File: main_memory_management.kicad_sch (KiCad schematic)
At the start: 21 parts

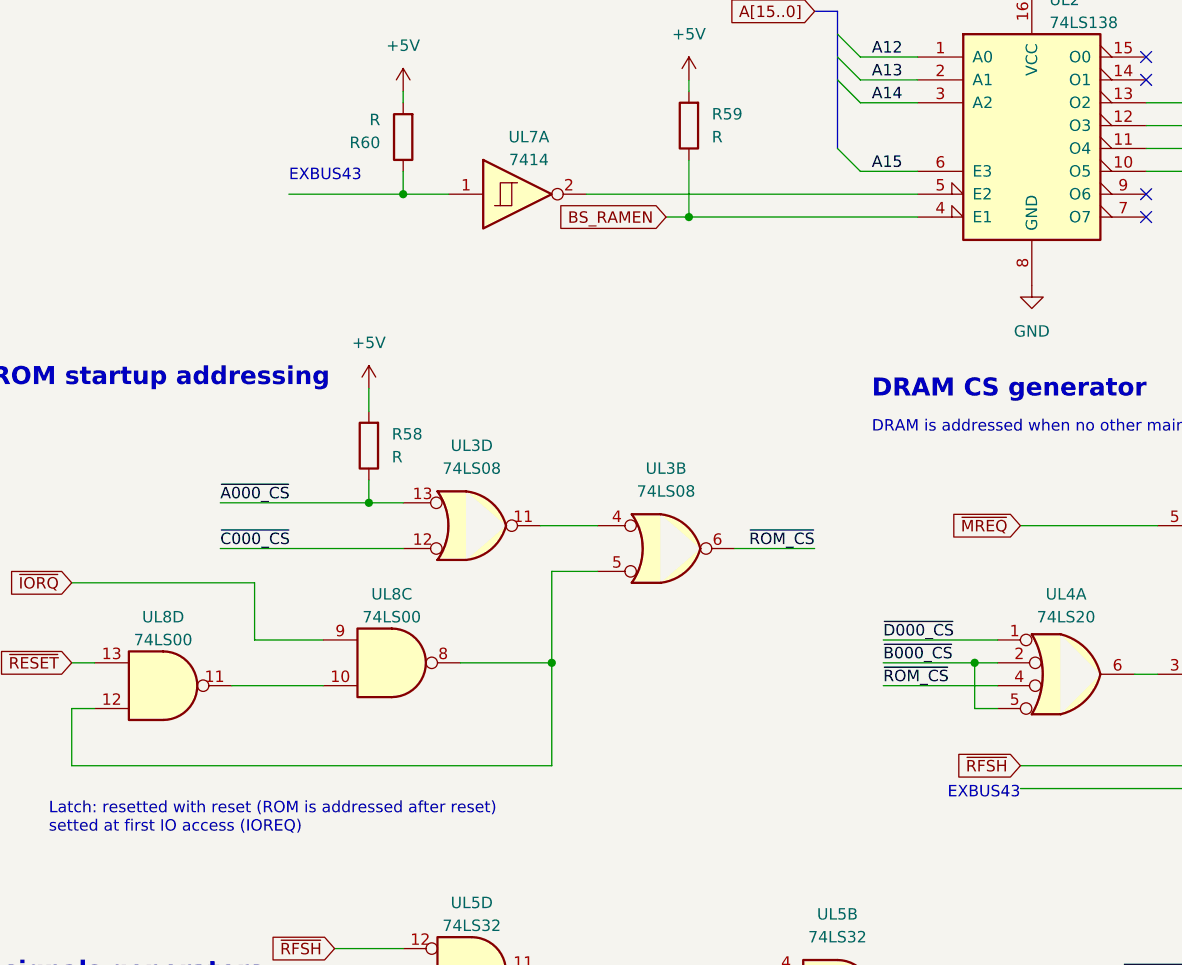
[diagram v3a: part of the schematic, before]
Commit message: pcb: added all the connector, 99% routed
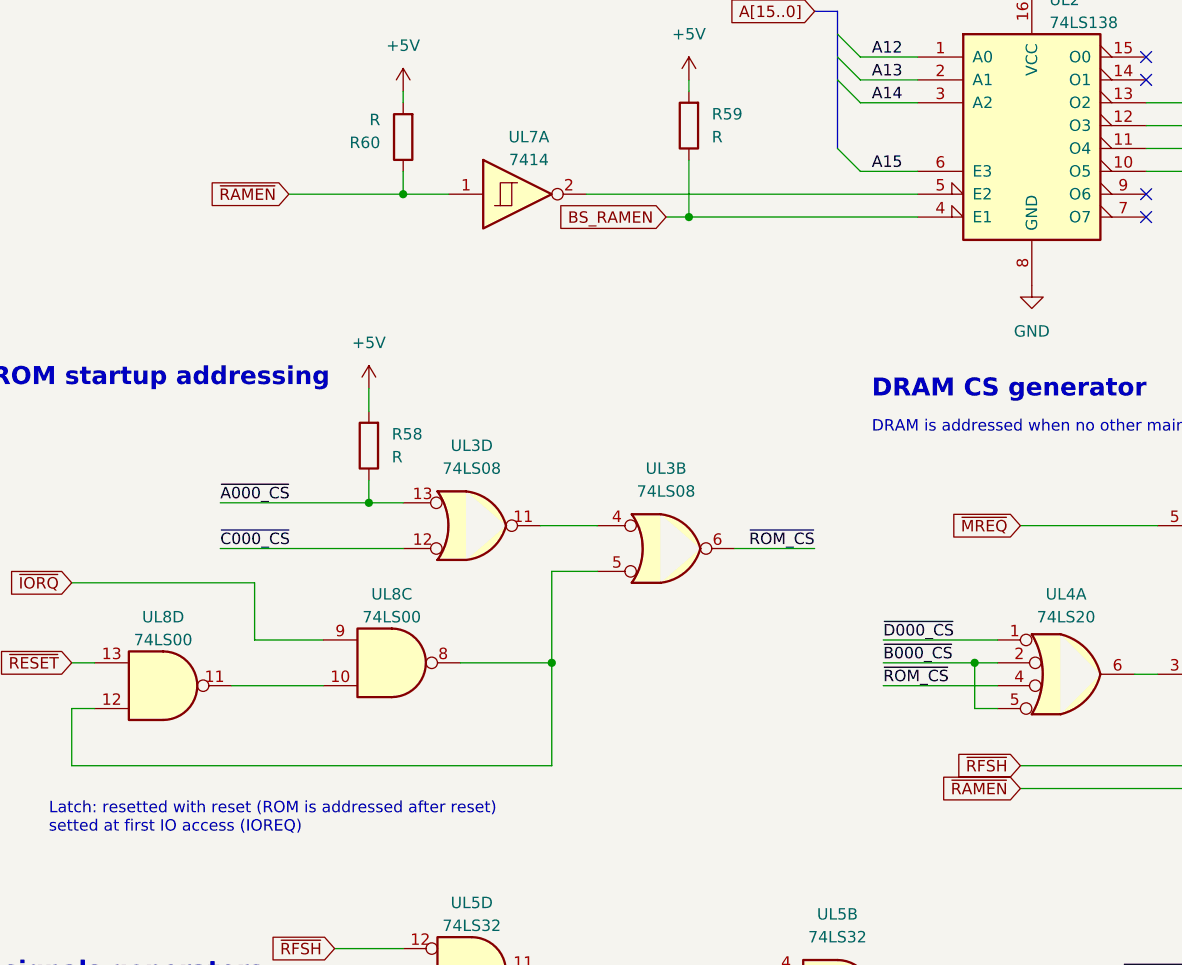
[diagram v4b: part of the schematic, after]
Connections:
- net ~{RAMEN}: now reaches UL4.13
- net ~{RAMEN}: now also R60.1, UL7.1
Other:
- note removed: "EXBUS43"
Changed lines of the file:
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@@
 		)
 	)
-	(text "EXBUS43\n"
-		(exclude_from_sim no)
-		(at 132.08 46.99 0)
-		(effects
-			(font
-				(size 1.27 1.27)
-			)
-			(justify left bottom)
-		)
-	)
 	(text "DRAM CS generator"
 		(exclude_from_sim no)
@@
 		)
 	)
-	(text "EXBUS43"
-		(exclude_from_sim no)
-		(at 213.36 115.57 0)
-		(effects
-			(font
-				(size 1.27 1.27)
-			)
-			(justify right bottom)
-		)
-	)
 	(text "DRAM is addressed when no other main memory are addressed"
 		(exclude_from_sim no)
@@
 		)
 	)
+	(global_label "~{RAMEN}"
+		(shape input)
+		(at 132.08 48.26 180)
+		(fields_autoplaced yes)
+		(effects
+			(font
+				(size 1.27 1.27)
+			)
+			(justify right)
+		)
+		(property "Intersheetrefs" "${INTERSHEET_REFS}"
+			(at 122.8053 48.26 0)
+			(effects
+				(font
+					(size 1.27 1.27)
+				)
+				(justify right)
+				(hide yes)
+			)
+		)
+	)
 	(global_label "~{RAS}"
 		(shape output)
@@
 			(effects
 				(font
+					(size 1.27 1.27)
+				)
+				(justify right)
+				(hide yes)
+			)
+		)
+	)
+	(global_label "~{RAMEN}"
+		(shape input)
+		(at 213.36 114.3 180)
+		(fields_autoplaced yes)
+		(effects
+			(font
+				(size 1.27 1.27)
+			)
+			(justify right)
+		)
+		(property "Intersheetrefs" "${INTERSHEET_REFS}"
+			(at 204.0853 114.3 0)
+			(effects
+				(font

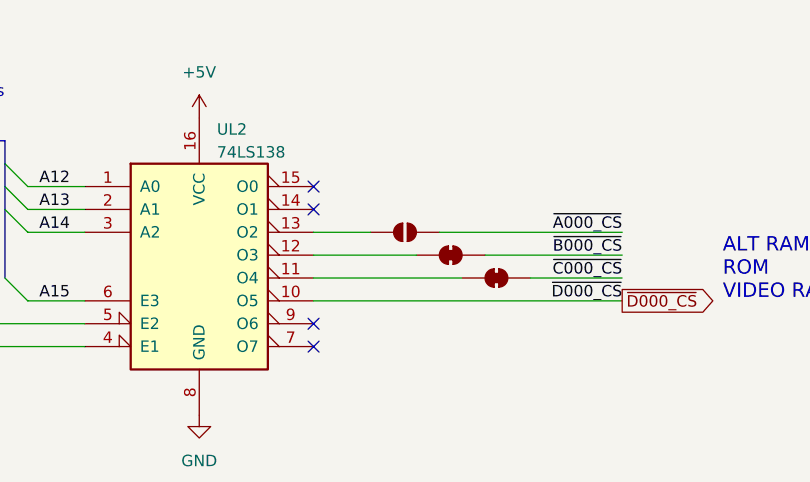
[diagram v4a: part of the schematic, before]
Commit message: pcb: proper symbols for MAP and MAINCLK
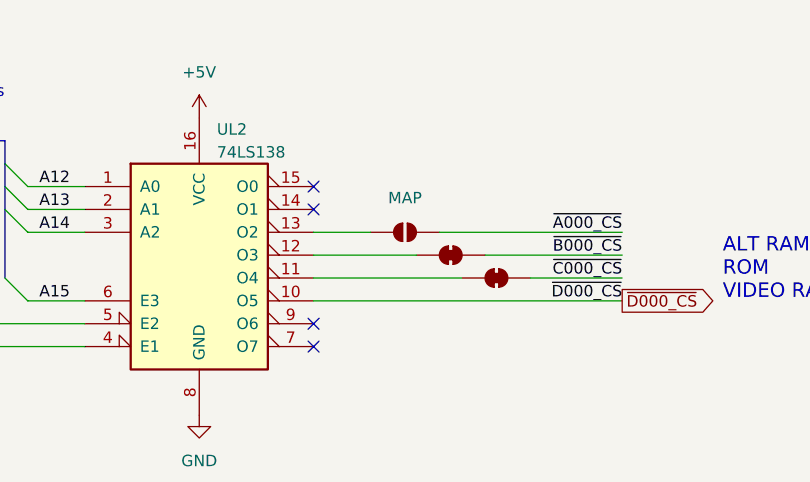
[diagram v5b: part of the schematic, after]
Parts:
- removed MAP1: SolderJumper_2_Open, Connector_PinHeader_2.54mm:PinHeader_2x01_P2.54mm_Vertical, symbol Jumper:SolderJumper_2_Open
- removed MAP2, MAP3: SolderJumper_2_Bridged, Connector_PinHeader_2.54mm:PinHeader_2x01_P2.54mm_Vertical, symbol Jumper:SolderJumper_2_Bridged
- added JP4: MAP, Ceda:MAP, symbol ceda:MAP
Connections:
- net ~{A000_CS}: now also JP4.2 (B)
- net ~{B000_CS}: now also JP4.4 (D)
- net ~{C000_CS}: now also JP4.6 (F)
- net at UL2.11 (O4): now also JP4.5 (E)
- net at UL2.12 (O3): now also JP4.3 (C)
- net at UL2.13 (O2): now also JP4.1 (A)
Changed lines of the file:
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@@
-	)
-	(symbol
-		(lib_id "Jumper:SolderJumper_2_Open")
-		(at 237.49 38.1 0)
-		(unit 1)
-		(exclude_from_sim no)
-		(in_bom yes)
-		(on_board yes)
-		(dnp no)
-		(fields_autoplaced yes)
-		(property "Reference" "MAP1"
-			(at 238.125 40.64 90)
-			(effects
-				(font
-					(size 1.27 1.27)
-				)
-				(justify right)
-				(hide yes)
-			)
-		)
-		(property "Value" "SolderJumper_2_Open"
-			(at 235.585 40.64 90)
-			(effects
-				(font
-					(size 1.27 1.27)
-				)
-				(justify right)
-				(hide yes)
-			)
-		)
-		(property "Footprint" "Connector_PinHeader_2.54mm:PinHeader_2x01_P2.54mm_Vertical"
-			(at 237.49 38.1 0)
-			(effects
-				(font
-					(size 1.27 1.27)
-				)
-				(hide yes)
-			)
-		)
-		(property "Datasheet" "~"
-			(at 237.49 38.1 0)
-			(effects
-				(font
-					(size 1.27 1.27)
-				)
-				(hide yes)
-			)
-		)
-		(property "Description" ""
-			(at 237.49 38.1 0)
-			(effects
-				(font
-					(size 1.27 1.27)
-				)
-			)
-		)
-		(pin "1"
-		)
-		(pin "2"
-		)
-		(instances
-			(project "ceda"
-				(path "/12a6dbe3-008d-4c5b-88f6-9f1c816060be/4fdb1b90-7ad1-4fa0-9b13-7b81abbda2ba"
-					(reference "MAP1")
-					(unit 1)
-				)
-			)
-		)
 	)
 	(symbol
@@
 	)
 	(symbol
+		(lib_id "ceda:MAP")
+		(at 247.65 43.18 0)
+		(unit 3)
+		(exclude_from_sim no)
+		(in_bom yes)
+		(on_board yes)
+		(dnp no)
+		(fields_autoplaced yes)
+		(property "Reference" "JP4"
+			(at 247.65 36.83 0)
+			(effects
+				(font
+					(size 1.27 1.27)
+				)
+				(hide yes)
+			)
+		)
+		(property "Value" "MAP"
+			(at 247.65 39.37 0)
+			(effects
+				(font
+					(size 1.27 1.27)
+				)
+				(hide yes)
+			)
+		)
+		(property "Footprint" "Ceda:MAP"
+			(at 247.65 39.624 0)
+			(effects
+				(font
+					(size 1.27 1.27)
+				)
+				(hide yes)
+			)
+		)
+		(property "Datasheet" "~"
+			(at 247.65 38.1 0)
+			(effects
+				(font
+					(size 1.27 1.27)
+				)
+				(hide yes)
+			)
+		)
+		(property "Description" ""
+			(at 247.65 43.18 0)
+			(effects
+				(font
+					(size 1.27 1.27)
+				)
+				(hide yes)
+			)
+		)
+		(pin "1"
+		)
+		(pin "6"
+		)
+		(pin "5"
+		)
+		(pin "4"
+		)
+		(pin "3"
+		)
+		(pin "2"
+		)
+		(instances
+			(project ""
+				(path "/12a6dbe3-008d-4c5b-88f6-9f1c816060be/4fdb1b90-7ad1-4fa0-9b13-7b81abbda2ba"
+					(reference "JP4")
+					(unit 3)
+				)
+			)
+		)
+	)
+	(symbol
 		(lib_id "power:+5V")
 		(at 29.21 68.58 90)
@@
 	)
 	(symbol
+		(lib_id "ceda:MAP")
+		(at 242.57 40.64 0)
+		(unit 2)
+		(exclude_from_sim no)
+		(in_bom yes)
+		(on_board yes)
+		(dnp no)
+		(fields_autoplaced yes)
+		(property "Reference" "JP4"
+			(at 242.57 34.29 0)
+			(effects
+				(font
+					(size 1.27 1.27)
+				)
+				(hide yes)
+			)
+		)
+		(property "Value" "MAP"
+			(at 242.57 36.83 0)
+			(effects
+				(font
+					(size 1.27 1.27)
+				)
+				(hide yes)
+			)
+		)
+		(property "Footprint" "Ceda:MAP"
+			(at 242.57 37.084 0)
+			(effects
+				(font
+					(size 1.27 1.27)
+				)
+				(hide yes)
+			)
+		)
+		(property "Datasheet" "~"
+			(at 242.57 35.56 0)
+			(effects
+				(font
+					(size 1.27 1.27)
+				)
+				(hide yes)
+			)
+		)
+		(property "Description" ""
+			(at 242.57 40.64 0)
+			(effects
+				(font
+					(size 1.27 1.27)
+				)
+				(hide yes)
+			)
+		)
+		(pin "1"
+		)
+		(pin "6"
+		)
+		(pin "5"
+		)
+		(pin "4"
+		)
+		(pin "3"
+		)
+		(pin "2"
+		)
+		(instances
+			(project ""
+				(path "/12a6dbe3-008d-4c5b-88f6-9f1c816060be/4fdb1b90-7ad1-4fa0-9b13-7b81abbda2ba"
+					(reference "JP4")
+					(unit 2)
+				)
+			)
+		)
+	)
+	(symbol
 		(lib_id "74xx:74LS14")
 		(at 157.48 48.26 0)
@@
 	)
 	(symbol
-		(lib_id "Jumper:SolderJumper_2_Bridged")
-		(at 247.65 43.18 0)
-		(unit 1)
-		(exclude_from_sim no)
-		(in_bom yes)
-		(on_board yes)
-		(dnp no)
-		(fields_autoplaced yes)
-		(property "Reference" "MAP3"
-			(at 247.65 38.1 0)
-			(effects
-				(font
-					(size 1.27 1.27)
-				)
-				(hide yes)
-			)
-		)
-		(property "Value" "SolderJumper_2_Bridged"
-			(at 247.65 40.64 0)
-			(effects
-				(font
-					(size 1.27 1.27)
-				)
-				(hide yes)
-			)
-		)
-		(property "Footprint" "Connector_PinHeader_2.54mm:PinHeader_2x01_P2.54mm_Vertical"
-			(at 247.65 43.18 0)
-			(effects
-				(font
-					(size 1.27 1.27)
-				)
-				(hide yes)
-			)
-		)
-		(property "Datasheet" "~"
-			(at 247.65 43.18 0)
-			(effects
-				(font
-					(size 1.27 1.27)
-				)
-				(hide yes)
-			)
-		)
-		(property "Description" ""
-			(at 247.65 43.18 0)
-			(effects
-				(font
-					(size 1.27 1.27)
-				)
-			)
-		)
-		(pin "1"
-		)
-		(pin "2"
-		)
-		(instances
-			(project "ceda"
-				(path "/12a6dbe3-008d-4c5b-88f6-9f1c816060be/4fdb1b90-7ad1-4fa0-9b13-7b81abbda2ba"
-					(reference "MAP3")
-					(unit 1)
-				)
-			)
-		)
-	)
-	(symbol
 		(lib_id "power:+5V")
 		(at 144.78 36.83 0)
@@
 	)
 	(symbol
-		(lib_id "Jumper:SolderJumper_2_Bridged")
-		(at 242.57 40.64 0)
-		(unit 1)
-		(exclude_from_sim no)
-		(in_bom yes)
-		(on_board yes)
-		(dnp no)
-		(fields_autoplaced yes)
-		(property "Reference" "MAP2"
-			(at 242.57 35.56 0)
-			(effects
-				(font
-					(size 1.27 1.27)
-				)
-				(hide yes)
-			)
-		)
-		(property "Value" "SolderJumper_2_Bridged"
-			(at 242.57 38.1 0)
-			(effects
-				(font
-					(size 1.27 1.27)
-				)
-				(hide yes)
-			)
-		)
-		(property "Footprint" "Connector_PinHeader_2.54mm:PinHeader_2x01_P2.54mm_Vertical"
-			(at 242.57 40.64 0)
-			(effects
-				(font
-					(size 1.27 1.27)
-				)
-				(hide yes)
-			)
-		)
-		(property "Datasheet" "~"
-			(at 242.57 40.64 0)
-			(effects
-				(font
-					(size 1.27 1.27)
-				)
-				(hide yes)
-			)
-		)
-		(property "Description" ""
-			(at 242.57 40.64 0)
-			(effects
-				(font
-					(size 1.27 1.27)
-				)
-			)
-		)
-		(pin "1"
-		)
-		(pin "2"
-		)
-		(instances
-			(project "ceda"
-				(path "/12a6dbe3-008d-4c5b-88f6-9f1c816060be/4fdb1b90-7ad1-4fa0-9b13-7b81abbda2ba"
-					(reference "MAP2")
-					(unit 1)
-				)
-			)
-		)
-	)
-	(symbol
 		(lib_id "power:+5V")
 		(at 50.8 97.79 0)
@@
 					(unit 1)
 				)
+			)
+		)
+	)
+	(symbol
+		(lib_id "ceda:MAP")
+		(at 237.49 38.1 0)
+		(unit 1)
+		(exclude_from_sim no)
+		(in_bom yes)
+		(on_board yes)
+		(dnp no)
+		(fields_autoplaced yes)
+		(property "Reference" "JP4"
+			(at 237.49 31.75 0)
+			(effects
+				(font
+					(size 1.27 1.27)
+				)
+				(hide yes)
+			)
+		)
+		(property "Value" "MAP"
+			(at 237.49 34.29 0)
+			(effects
+				(font
+					(size 1.27 1.27)
+				)
+			)
+		)
+		(property "Footprint" "Ceda:MAP"
+			(at 237.49 34.544 0)
+			(effects
+				(font
+					(size 1.27 1.27)
+				)
+				(hide yes)
+			)
+		)
+		(property "Datasheet" "~"
+			(at 237.49 33.02 0)
+			(effects
+				(font
+					(size 1.27 1.27)
+				)
+				(hide yes)
+			)
+		)
+		(property "Description" ""
+			(at 237.49 38.1 0)
+			(effects
+				(font
+					(size 1.27 1.27)
+				)
+				(hide yes)
+			)
+		)
+		(pin "1"
+		)
+		(pin "6"
+		)
+		(pin "5"
+		)
+		(pin "4"
+		)
+		(pin "3"
+		)
+		(pin "2"
+		)
+		(instances
+			(project ""
+				(path "/12a6dbe3-008d-4c5b-88f6-9f1c816060be/4fdb1b90-7ad1-4fa0-9b13-7b81abbda2ba"
+					(reference "JP4")
+					(unit 1)
+				)
